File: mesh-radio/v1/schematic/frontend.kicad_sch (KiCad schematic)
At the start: 51 parts, among them J4 U.FL-R-SMT-1(80), U10 QPA9510TR7, U11 SKY13330-397LF, U12 BGA7L1BN6E6327XTSA1

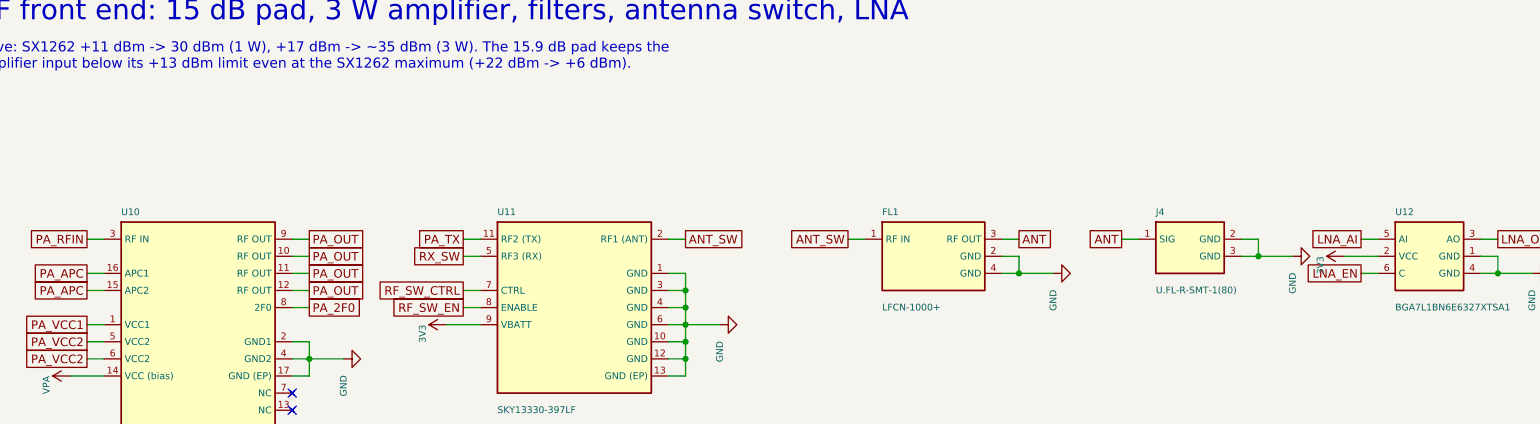
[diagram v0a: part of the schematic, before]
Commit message: Mesh Radio v1: fix every design-review finding, add the part audit
An independent review of the schematic found two critical and nine further
issues; all are fixed in src/circuit.py:
- reverse-battery FET gate now returns to the cell's own minus terminal, so
  a backwards cell stays isolated even while USB/solar/drone power the board
- solar and drone inputs: reverse-blocking Schottky + 22 V flat-clamp TVS
  (the 15 V TVS would have failed on a 12 V panel); 4.7 V clamp on every
  eFuse EN/UVLO pin so 20 V on an input stays inside its rating
- ideal diode (LM66100) holds VSYS on the cell when a 3 W burst trips the
  charger's 3.0 V battery disconnect
- charge LED moved to STAT2 (charging), USB cut-off lowered to 5.4 V,
  charger /CE on a GPIO for firmware temperature control, -40 C TCXO,
  power mux on only with the amplifier, header VSYS pin removed
- firmware ceilings documented: SX1262 +20 dBm, amplifier 3.6 V by default

docs/part-audit.md: all 125 lines checked at DigiKey and LCSC (genuine
LCSC numbers, DigiKey numbers, second sources for out-of-stock lines);
parts cost about $76 at 10 boards, $58 at 100.

Schematic regenerated: ERC 0 violations, netlist equals circuit.py.

Co-Authored-By: Claude Opus 5.5 <noreply@anthropic.com>
Claude-Session: https://claude.ai/code/session_015TBB2ThqxHSgA8MkFosmn9
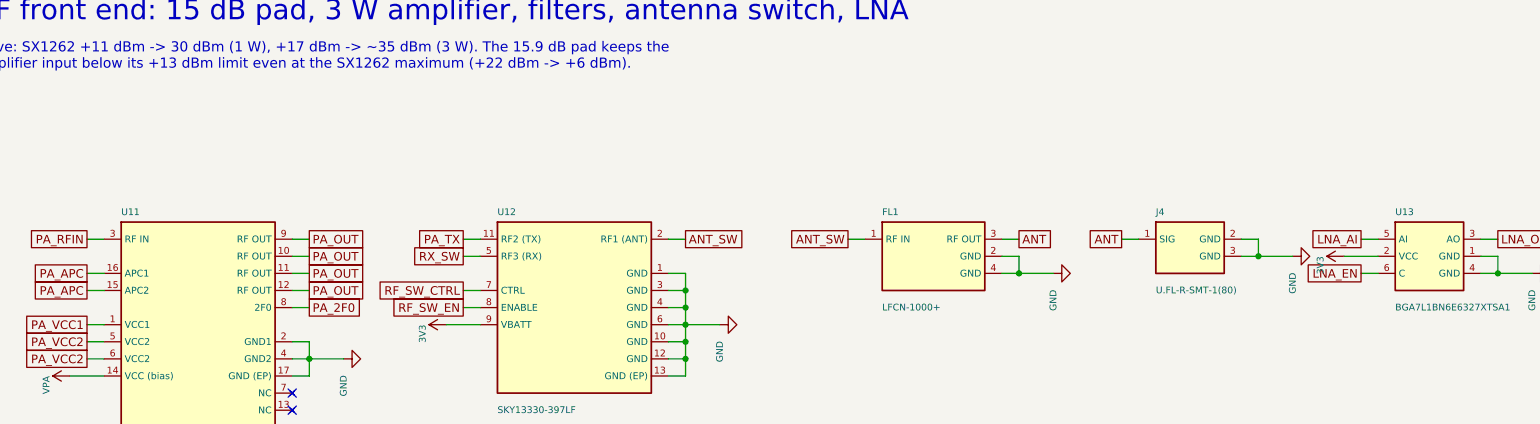
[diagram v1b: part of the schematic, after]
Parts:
- removed U10: QPA9510TR7, og:QFN-16_3x3_QPA9510, symbol og:QPA9510
- added U13: BGA7L1BN6E6327XTSA1, og:TSNP-6_L1.1-W0.7-P0.40-BL, symbol og:BGA7L1BN6
- C56, C66, C72: DigiKey (none) -> 490-14446-1-ND
- C57, C61, C68, C69, C83: DigiKey (none) -> 1276-1028-1-ND
- C58, C62, C71, C84, C85: DigiKey (none) -> 490-3244-1-ND
- C59, C64, C65: DigiKey (none) -> 490-17672-1-ND
- C60, C70: DigiKey (none) -> 1276-1044-1-ND
- C63: DigiKey (none) -> 490-3117-1-ND
- C67: DigiKey (none) -> 490-8087-1-ND
- C73: DigiKey (none) -> 490-14794-1-ND
- C74: DigiKey (none) -> 490-6086-1-ND
- C75: DigiKey (none) -> 490-7162-1-ND
- C76: DigiKey (none) -> 490-5900-1-ND
- C77: DigiKey (none) -> 490-8126-1-ND
- C78: DigiKey (none) -> 490-5282-1-ND
- C79: DigiKey (none) -> 490-GQM2195C2E4R3BB12DCT-ND
- C80: DigiKey (none) -> 490-GQM2195C2ER70WB12DCT-ND
- C81: DigiKey (none) -> 490-5286-1-ND
- C82: DigiKey (none) -> 490-5922-1-ND
- C86: DigiKey (none) -> 1276-1001-1-ND
- FB1, FB2: DigiKey (none) -> 490-5176-1-ND
- FL1: DigiKey (none) -> 3157-LFCN-1000+CT-ND
- J4: DigiKey (none) -> 26-U.FL-R-SMT-1(80)CT-ND
- L12: DigiKey (none) -> 490-6859-1-ND
- L13: DigiKey (none) -> 490-8388-1-ND
- L15: DigiKey (none) -> 490-1159-1-ND
- L16: DigiKey (none) -> 490-6832-1-ND
- L17: DigiKey (none) -> 490-1162-1-ND
- L18: DigiKey (none) -> 490-1154-1-ND
- L19: DigiKey (none) -> 490-6766-1-ND
- R41, R43: DigiKey (none) -> 311-68.0CRCT-ND
- R42: DigiKey (none) -> 311-150CRCT-ND
- R44: DigiKey (none) -> 311-220KLRCT-ND
- R45: DigiKey (none) -> 311-330KLRCT-ND
- U11: value SKY13330-397LF -> QPA9510TR7; footprint og:QFN-12_L2.0-W2.0-P0.50-BL-EP0.8 -> og:QFN-16_3x3_QPA9510; symbol og:SKY13330 -> og:QPA9510; DigiKey (none) -> 2312-QPA9510TR7CT-ND; LCSC C2654715 -> C52059849; MPN SKY13330-397LF -> QPA9510TR7; Manufacturer Skyworks Solutions -> Qorvo
- U12: value BGA7L1BN6E6327XTSA1 -> SKY13330-397LF; footprint og:TSNP-6_L1.1-W0.7-P0.40-BL -> og:QFN-12_L2.0-W2.0-P0.50-BL-EP0.8; symbol og:BGA7L1BN6 -> og:SKY13330; DigiKey (none) -> 863-1643-1-ND; LCSC C534173 -> C2654715; MPN BGA7L1BN6E6327XTSA1 -> SKY13330-397LF; Manufacturer Infineon Technologies -> Skyworks Solutions
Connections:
- net 3V3: now also U12.9 (VBATT), U13.2 (VCC); no longer U11.9 (VBATT), U12.2 (VCC)
- net ANT_SW: now also U12.2 (RF1 (ANT)); no longer U11.2 (RF1 (ANT))
- net GND: now also U11.17 (GND (EP)), U11.2 (GND1), U12.10 (GND), U12.12 (GND), U12.13 (GND (EP)), U12.3 (GND), U12.6 (GND), U13.1 (GND), U13.4 (GND); no longer U11.1 (GND), U11.10 (GND), U11.12 (GND), U11.13 (GND (EP)), U11.3 (GND), U11.6 (GND)
- net LNA_AI: now also U13.5 (AI); no longer U12.5 (AI)
- net LNA_EN: now also U13.6 (C); no longer U12.6 (C)
- net LNA_OUT: now also U13.3 (AO); no longer U12.3 (AO)
- net PA_2F0: now also U11.8 (2F0)
- net PA_APC: now also U11.15 (APC2), U11.16 (APC1)
- net PA_OUT: now also U11.10 (RF OUT), U11.11 (RF OUT), U11.12 (RF OUT), U11.9 (RF OUT)
- net PA_RFIN: now also U11.3 (RF IN)
- net PA_TX: now also U12.11 (RF2 (TX)); no longer U11.11 (RF2 (TX))
- net PA_VCC1: now also U11.1 (VCC1)
- net PA_VCC2: now also U11.5 (VCC2), U11.6 (VCC2)
- net RF_SW_CTRL: now also U12.7 (CTRL); no longer U11.7 (CTRL)
- net RF_SW_EN: now also U12.8 (ENABLE); no longer U11.8 (ENABLE)
- net RX_SW: now also U12.5 (RF3 (RX)); no longer U11.5 (RF3 (RX))
- net VPA: now also U11.14 (VCC (bias))

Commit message: Mesh radio v1: RF fixes from sim/rf (3 W heating, pad power, filter loss)
sim/rf found three failures at 3 W; fixed with the same part count:
- the amplifier output-match inductor and the two harmonic-filter
  inductors ran 1.1-2.7x past their rated self-heating: now Murata
  LQW2BAN 0805 wire-wound (2 A class), 3.6 / 3.2 / 3.2 nH;
- the harmonic filter's values move (2.0, 3.2 nH || 3.6 pF, 1.3,
  3.2 nH || 1.3 pF, 0.9 pF, Murata GQM1875 250 V C0G): 0.3 dB less loss,
  so 3 W reaches the U.FL; 2f-5f harmonic yield stays 100 % at
  -40..85 C;
- the pad's first 68 R reached 114 % of its rating at +22 dBm drive and
  85 C: now Vishay RCS0805 anti-surge, 0.4 W;
- the Bluetooth match's 0.8 pF is the +-0.05 pF grade (100 % yield).
Schematic regenerated: ERC 0, netlist equals circuit.py.  sim/rf
snapshot included; the open-antenna and 6f-10f checks are still running.

Co-Authored-By: Claude Opus 5.5 <noreply@anthropic.com>
Claude-Session: https://claude.ai/code/session_015TBB2ThqxHSgA8MkFosmn9
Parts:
- C77: value 3.3pF -> 2.0pF; DigiKey 490-8126-1-ND -> (none); LCSC C882553 -> C6867410; MPN GQM1875C2E3R3BB12D -> GQM1875C2E2R0BB12D
- C78: value 1.5pF -> 3.6pF; footprint og:C_0805 -> og:C_0603; DigiKey 490-5282-1-ND -> (none); LCSC C2173009 -> C2178747; MPN GQM2195C2E1R5BB12D -> GQM1875C2E3R6BB12D
- C79: value 4.3pF -> 1.3pF; footprint og:C_0805 -> og:C_0603; DigiKey 490-GQM2195C2E4R3BB12DCT-ND -> (none); LCSC C668332 -> C3901219; MPN GQM2195C2E4R3BB12D -> GQM1875C2E1R3BB12D
- C80: value 0.7pF -> 1.3pF; footprint og:C_0805 -> og:C_0603; DigiKey 490-GQM2195C2ER70WB12DCT-ND -> (none); LCSC C3908487 -> C3901219; MPN GQM2195C2ER70WB12D -> GQM1875C2E1R3BB12D
- C81: value 2.7pF -> 0.9pF; footprint og:C_0805 -> og:C_0603; DigiKey 490-5286-1-ND -> (none); LCSC C668330 -> C1865143; MPN GQM2195C2E2R7BB12D -> GQM1875C2ER90BB12D
- L15: footprint og:L_0603 -> og:L_0805; DigiKey 490-1159-1-ND -> (none); LCSC C341694 -> C2045110; MPN LQW18AN3N6D00D -> LQW2BAN3N6J00L
- L16: value 5.1nH -> 3.2nH; footprint og:L_0402 -> og:L_0805; DigiKey 490-6832-1-ND -> (none); LCSC C113117 -> C2043110; MPN LQW15AN5N1C00D -> LQW2BAN3N2J00L
- L17: value 4.7nH -> 3.2nH; footprint og:L_0603 -> og:L_0805; DigiKey 490-1162-1-ND -> (none); LCSC C98078 -> C2043110; MPN LQW18AN4N7D00D -> LQW2BAN3N2J00L
- R41: DigiKey 311-68.0CRCT-ND -> (none); LCSC C137498 -> C2114866; MPN RC0805FR-0768RL -> RCS080568R0FKEA; Manufacturer Yageo -> Vishay Dale
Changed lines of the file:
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@@
 			)
 		)
-		(property "MPN" "RC0805FR-0768RL"
+		(property "MPN" "RCS080568R0FKEA"
 			(at 25.4 116.84 0)
 			(effects
@@
 			)
 		)
-		(property "Manufacturer" "Yageo"
-			(at 25.4 116.84 0)
-			(effects
-				(font
-					(size 1.27 1.27)
-				)
-				(hide yes)
-			)
-		)
-		(property "DigiKey" "311-68.0CRCT-ND"
+		(property "Manufacturer" "Vishay Dale"
 			(at 25.4 116.84 0)
 			(effects
@@
 			)
 		)
-		(property "LCSC" "C137498"
+		(property "LCSC" "C2114866"
 			(at 25.4 116.84 0)
 			(effects
@@
 			)
 		)
-		(property "Description" "Resistor 68R 1% 0805"
+		(property "Description" "Resistor 68R 1% 0.4 W anti-surge 0805"
 			(at 25.4 116.84 0)
 			(effects
@@
 			)
 		)
-		(property "Value" "3.3pF"
+		(property "Value" "2.0pF"
 			(at 332 115.9 0)
 			(effects
@@
 			)
 		)
-		(property "MPN" "GQM1875C2E3R3BB12D"
+		(property "MPN" "GQM1875C2E2R0BB12D"
 			(at 330.2 114.3 0)
 			(effects
@@
 			)
 		)
-		(property "DigiKey" "490-8126-1-ND"
+		(property "LCSC" "C6867410"
 			(at 330.2 114.3 0)
 			(effects
@@
 			)
 		)
-		(property "LCSC" "C882553"
-			(at 330.2 114.3 0)
-			(effects
-				(font
-					(size 1.27 1.27)
-				)
-				(hide yes)
-			)
-		)
-		(property "Description" "Capacitor 3.3pF 250V C0G high-Q 0603"
+		(property "Description" "Capacitor 2.0pF 250V C0G high-Q 0603"
 			(at 330.2 114.3 0)
 			(effects
@@
 			)
 		)
-		(property "Value" "4.3pF"
+		(property "Value" "1.3pF"
 			(at 344.7 115.9 0)
 			(effects
@@
 			)
 		)
-		(property "Footprint" "og:C_0805"
+		(property "Footprint" "og:C_0603"
 			(at 342.9 114.3 0)
 			(effects
@@
 			)
 		)
-		(property "MPN" "GQM2195C2E4R3BB12D"
+		(property "MPN" "GQM1875C2E1R3BB12D"
 			(at 342.9 114.3 0)
 			(effects
@@
 			)
 		)
-		(property "DigiKey" "490-GQM2195C2E4R3BB12DCT-ND"
+		(property "LCSC" "C3901219"
 			(at 342.9 114.3 0)
 			(effects
@@
 			)
 		)
-		(property "LCSC" "C668332"
-			(at 342.9 114.3 0)
-			(effects
-				(font
-					(size 1.27 1.27)
-				)
-				(hide yes)
-			)
-		)
-		(property "Description" "Capacitor 4.3pF 250V C0G high-Q 0805"
+		(property "Description" "Capacitor 1.3pF 250V C0G high-Q 0603"
 			(at 342.9 114.3 0)
 			(effects
@@
 			)
 		)
-		(property "Value" "2.7pF"
+		(property "Value" "0.9pF"
 			(at 357.4 115.9 0)
 			(effects
@@
 			)
 		)
-		(property "Footprint" "og:C_0805"
+		(property "Footprint" "og:C_0603"
 			(at 355.6 114.3 0)
 			(effects
@@
 			)
 		)
-		(property "MPN" "GQM2195C2E2R7BB12D"
+		(property "MPN" "GQM1875C2ER90BB12D"
 			(at 355.6 114.3 0)
 			(effects
@@
 			)
 		)
-		(property "DigiKey" "490-5286-1-ND"
+		(property "LCSC" "C1865143"
 			(at 355.6 114.3 0)
 			(effects
@@
 			)
 		)
-		(property "LCSC" "C668330"
-			(at 355.6 114.3 0)
-			(effects
-				(font
-					(size 1.27 1.27)
-				)
-				(hide yes)
-			)
-		)
-		(property "Description" "Capacitor 2.7pF 250V C0G high-Q 0805"
+		(property "Description" "Capacitor 0.9pF 250V C0G high-Q 0603"
 			(at 355.6 114.3 0)
 			(effects
@@
 			)
 		)
-		(property "Footprint" "og:L_0603"
+		(property "Footprint" "og:L_0805"
 			(at 215.9 180.34 0)
 			(effects
@@
 			)
 		)
-		(property "MPN" "LQW18AN3N6D00D"
+		(property "MPN" "LQW2BAN3N6J00L"
 			(at 215.9 180.34 0)
 			(effects
@@
 			)
 		)
-		(property "DigiKey" "490-1159-1-ND"
+		(property "LCSC" "C2045110"
 			(at 215.9 180.34 0)
 			(effects
@@
 			)
 		)
-		(property "LCSC" "C341694"
-			(at 215.9 180.34 0)
-			(effects
-				(font
-					(size 1.27 1.27)
-				)
-				(hide yes)
-			)
-		)
-		(property "Description" "Inductor 3.6nH 0603 wire-wound RF, amplifier output match"
+		(property "Description" "Inductor 3.6nH 0805 wire-wound RF 0805, amplifier output match"
 			(at 215.9 180.34 0)
 			(effects
@@
 			)
 		)
-		(property "Value" "5.1nH"
+		(property "Value" "3.2nH"
 			(at 294.64 183.34 0)
 			(effects
@@
 			)
 		)
-		(property "Footprint" "og:L_0402"
+		(property "Footprint" "og:L_0805"
 			(at 294.64 180.34 0)
 			(effects
@@
 			)
 		)
-		(property "MPN" "LQW15AN5N1C00D"
+		(property "MPN" "LQW2BAN3N2J00L"
 			(at 294.64 180.34 0)
 			(effects
@@
 			)
 		)
-		(property "DigiKey" "490-6832-1-ND"
+		(property "LCSC" "C2043110"
 			(at 294.64 180.34 0)
 			(effects
@@
 			)
 		)
-		(property "LCSC" "C113117"
-			(at 294.64 180.34 0)
-			(effects
-				(font
-					(size 1.27 1.27)
-				)
-				(hide yes)
-			)
-		)
-		(property "Description" "Inductor 5.1nH 0402 wire-wound RF"
+		(property "Description" "Inductor 3.2nH 0805 wire-wound RF 0805, harmonic filter"
 			(at 294.64 180.34 0)
 			(effects
@@
 			)
 		)
-		(property "Value" "1.5pF"
+		(property "Value" "3.6pF"
 			(at 332.74 183.34 0)
 			(effects
@@
 			)
 		)
-		(property "Footprint" "og:C_0805"
+		(property "Footprint" "og:C_0603"
 			(at 332.74 180.34 0)
 			(effects
@@
 			)
 		)
-		(property "MPN" "GQM2195C2E1R5BB12D"
+		(property "MPN" "GQM1875C2E3R6BB12D"
 			(at 332.74 180.34 0)
 			(effects
@@
 			)
 		)
-		(property "DigiKey" "490-5282-1-ND"
-			(at 332.74 180.34 0)
-			(effects
-				(font
-					(size 1.27 1.27)
-				)
-				(hide yes)
-			)
-		)
-		(property "LCSC" "C2173009"
+		(property "LCSC" "C2178747"
 			(at 332.74 180.34 0)
 			(effects
@@
 			)
 		)
-		(property "Description" "Capacitor 1.5pF 250V C0G high-Q 0805"
+		(property "Description" "Capacitor 3.6pF 250V C0G high-Q 0603"
 			(at 332.74 180.34 0)
 			(effects
@@
 			)
 		)
-		(property "Value" "4.7nH"
+		(property "Value" "3.2nH"
 			(at 43.18 196.04 0)
 			(effects
@@
 			)
 		)
-		(property "Footprint" "og:L_0603"
+		(property "Footprint" "og:L_0805"
 			(at 43.18 193.04 0)
 			(effects
@@
 			)
 		)
-		(property "MPN" "LQW18AN4N7D00D"
+		(property "MPN" "LQW2BAN3N2J00L"
 			(at 43.18 193.04 0)
 			(effects
@@
 			)
 		)
-		(property "DigiKey" "490-1162-1-ND"
+		(property "LCSC" "C2043110"
 			(at 43.18 193.04 0)
 			(effects
@@
 			)
 		)
-		(property "LCSC" "C98078"
-			(at 43.18 193.04 0)
-			(effects
-				(font
-					(size 1.27 1.27)
-				)
-				(hide yes)
-			)
-		)
-		(property "Description" "Inductor 4.7nH 0603 wire-wound RF, harmonic filter"
+		(property "Description" "Inductor 3.2nH 0805 wire-wound RF 0805, harmonic filter"
 			(at 43.18 193.04 0)
 			(effects
@@
 			)
 		)
-		(property "Value" "0.7pF"
+		(property "Value" "1.3pF"
 			(at 81.28 196.04 0)
 			(effects
@@
 			)
 		)
-		(property "Footprint" "og:C_0805"
+		(property "Footprint" "og:C_0603"
 			(at 81.28 193.04 0)
 			(effects
@@
 			)
 		)
-		(property "MPN" "GQM2195C2ER70WB12D"
+		(property "MPN" "GQM1875C2E1R3BB12D"
 			(at 81.28 193.04 0)
 			(effects
@@
 			)
 		)
-		(property "DigiKey" "490-GQM2195C2ER70WB12DCT-ND"
-			(at 81.28 193.04 0)
-			(effects
-				(font
-					(size 1.27 1.27)
-				)
-				(hide yes)
-			)
-		)
-		(property "LCSC" "C3908487"
+		(property "LCSC" "C3901219"
 			(at 81.28 193.04 0)
 			(effects
@@
 			)
 		)
-		(property "Description" "Capacitor 0.7pF 250V C0G high-Q 0805"
+		(property "Description" "Capacitor 1.3pF 250V C0G high-Q 0603"
 			(at 81.28 193.04 0)
 			(effects
